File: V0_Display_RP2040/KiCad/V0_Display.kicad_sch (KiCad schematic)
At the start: 39 parts, among them J1 GPIO, J2 I2C Header, J2 USB4105-GF-A, J3 SWD, J7 USB_Header, J8 Neopixel, SW6 Kill_SW, SW7 Rotary_Enc, U1 AP2127K-3.3, U2 W25Q16JVUXIQ, U3 74LVC1G17, U4 RP2040, Y1 12MHz

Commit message: Fix Footprints
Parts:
- J2: value USB4105-GF-A -> GT-USB-7010ASV; footprint footprints:USB4105-GF-A -> Connector_USB:USB_C_Receptacle_G-Switch_GT-USB-7010ASV
- R1, R11: value 10k -> 10K
- U3: footprint V0-Display:SOT-753 -> Package_TO_SOT_SMD:SOT-23-5
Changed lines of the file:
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@@
       (effects (font (size 1.27 1.27)))
     )
-    (property "Footprint" "V0-Display:SOT-753" (at 111.76 189.23 0)
+    (property "Footprint" "Package_TO_SOT_SMD:SOT-23-5" (at 111.76 189.23 0)
       (effects (font (size 1.27 1.27)) hide)
     )
@@
       (effects (font (size 1.524 1.524)) (justify left))
     )
-    (property "Value" "USB4105-GF-A" (at 118.11 91.44 0)
+    (property "Value" "GT-USB-7010ASV" (at 118.11 91.44 0)
       (effects (font (size 1.524 1.524)) (justify left))
     )
-    (property "Footprint" "footprints:USB4105-GF-A" (at 127 91.694 0)
+    (property "Footprint" "Connector_USB:USB_C_Receptacle_G-Switch_GT-USB-7010ASV" (at 127 91.694 0)
       (effects (font (size 1.524 1.524)) hide)
     )
@@
       (effects (font (size 1.27 1.27)))
     )
-    (property "Value" "10k" (at 149.86 106.68 90)
+    (property "Value" "10K" (at 149.86 106.68 90)
       (effects (font (size 1.27 1.27)))
     )
@@
       (effects (font (size 1.27 1.27)))
     )
-    (property "Value" "10k" (at 104.14 104.14 90)
-      (effects (font (size 1.27 1.27)))
-    )
+    (property "Value" "10K" (at 104.14 104.14 90)
+      (effects (font (size 1.27 1.27)))
+    )

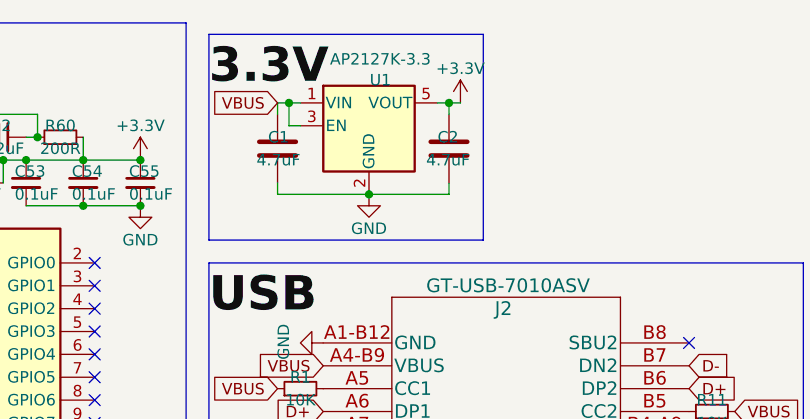
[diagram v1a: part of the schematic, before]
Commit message: Update Files
New 3.3V Regulator
"Fixed" Neopixel Level Shifter
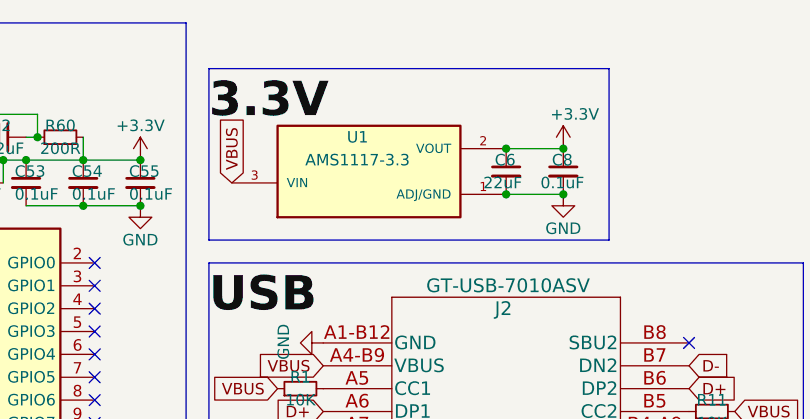
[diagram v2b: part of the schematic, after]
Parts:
- removed C1, C2: 4.7uF, Capacitor_SMD:C_0603_1608Metric, symbol Device:C
- removed U1: AP2127K-3.3, Package_TO_SOT_SMD:SOT-23-5, symbol V0_Display:AP2127K-3.3
- added C6: 22uF, Capacitor_SMD:C_0603_1608Metric, symbol Device:C_Small
- added C8: 0.1uF, Capacitor_SMD:C_0603_1608Metric, symbol Device:C_Small
- added U1: AMS1117-3.3, footprints:AMS1117-3.3, symbol AMS1117-3.3:AMS1117-3.3
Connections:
- net +3.3V: now also C6.1, C8.1, U1.2 (VOUT)
- net GND: now also C6.2, C8.2, U1.1 (ADJ/GND)
- net VCC: now also U1.3 (VIN)

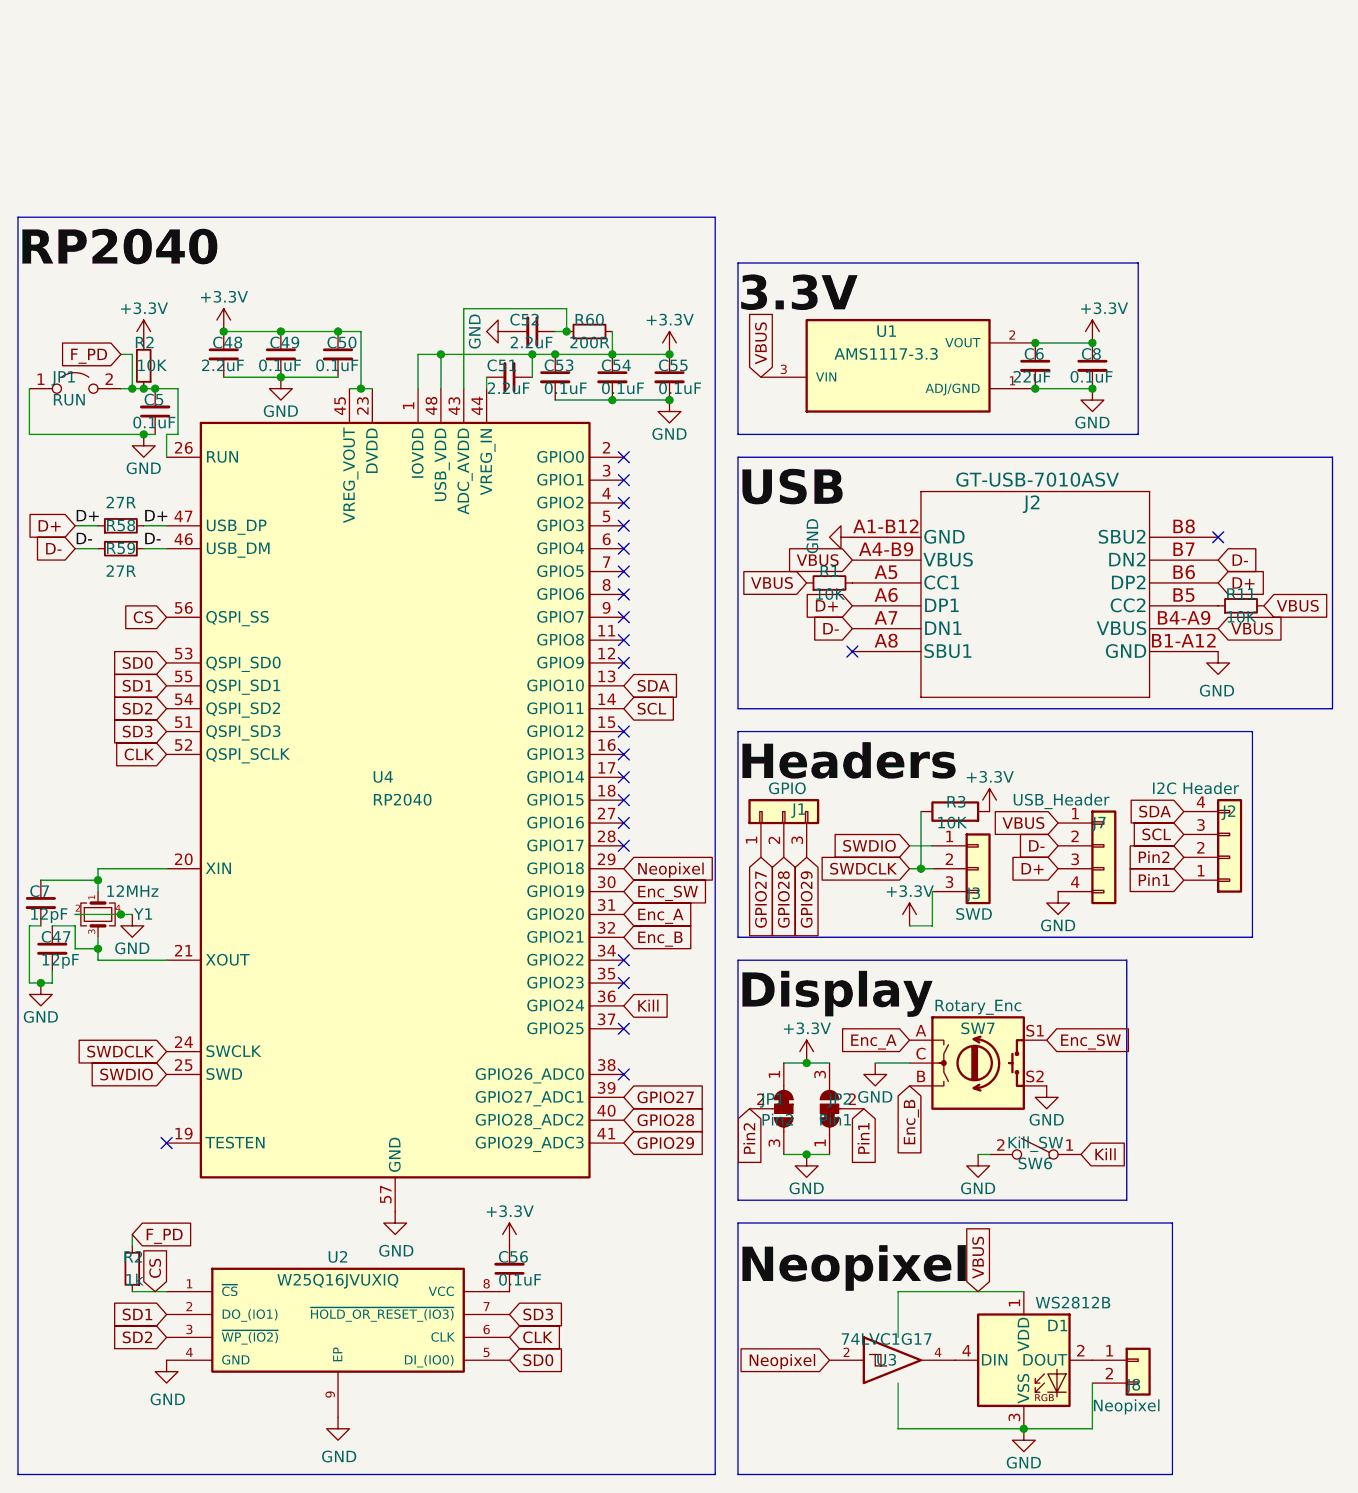
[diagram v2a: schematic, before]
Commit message: Rev 1.1
Fix Vreg-Out Problem
Change to AMS1117-3.3
22uF Input Capacitor on VBUS (5V IN)
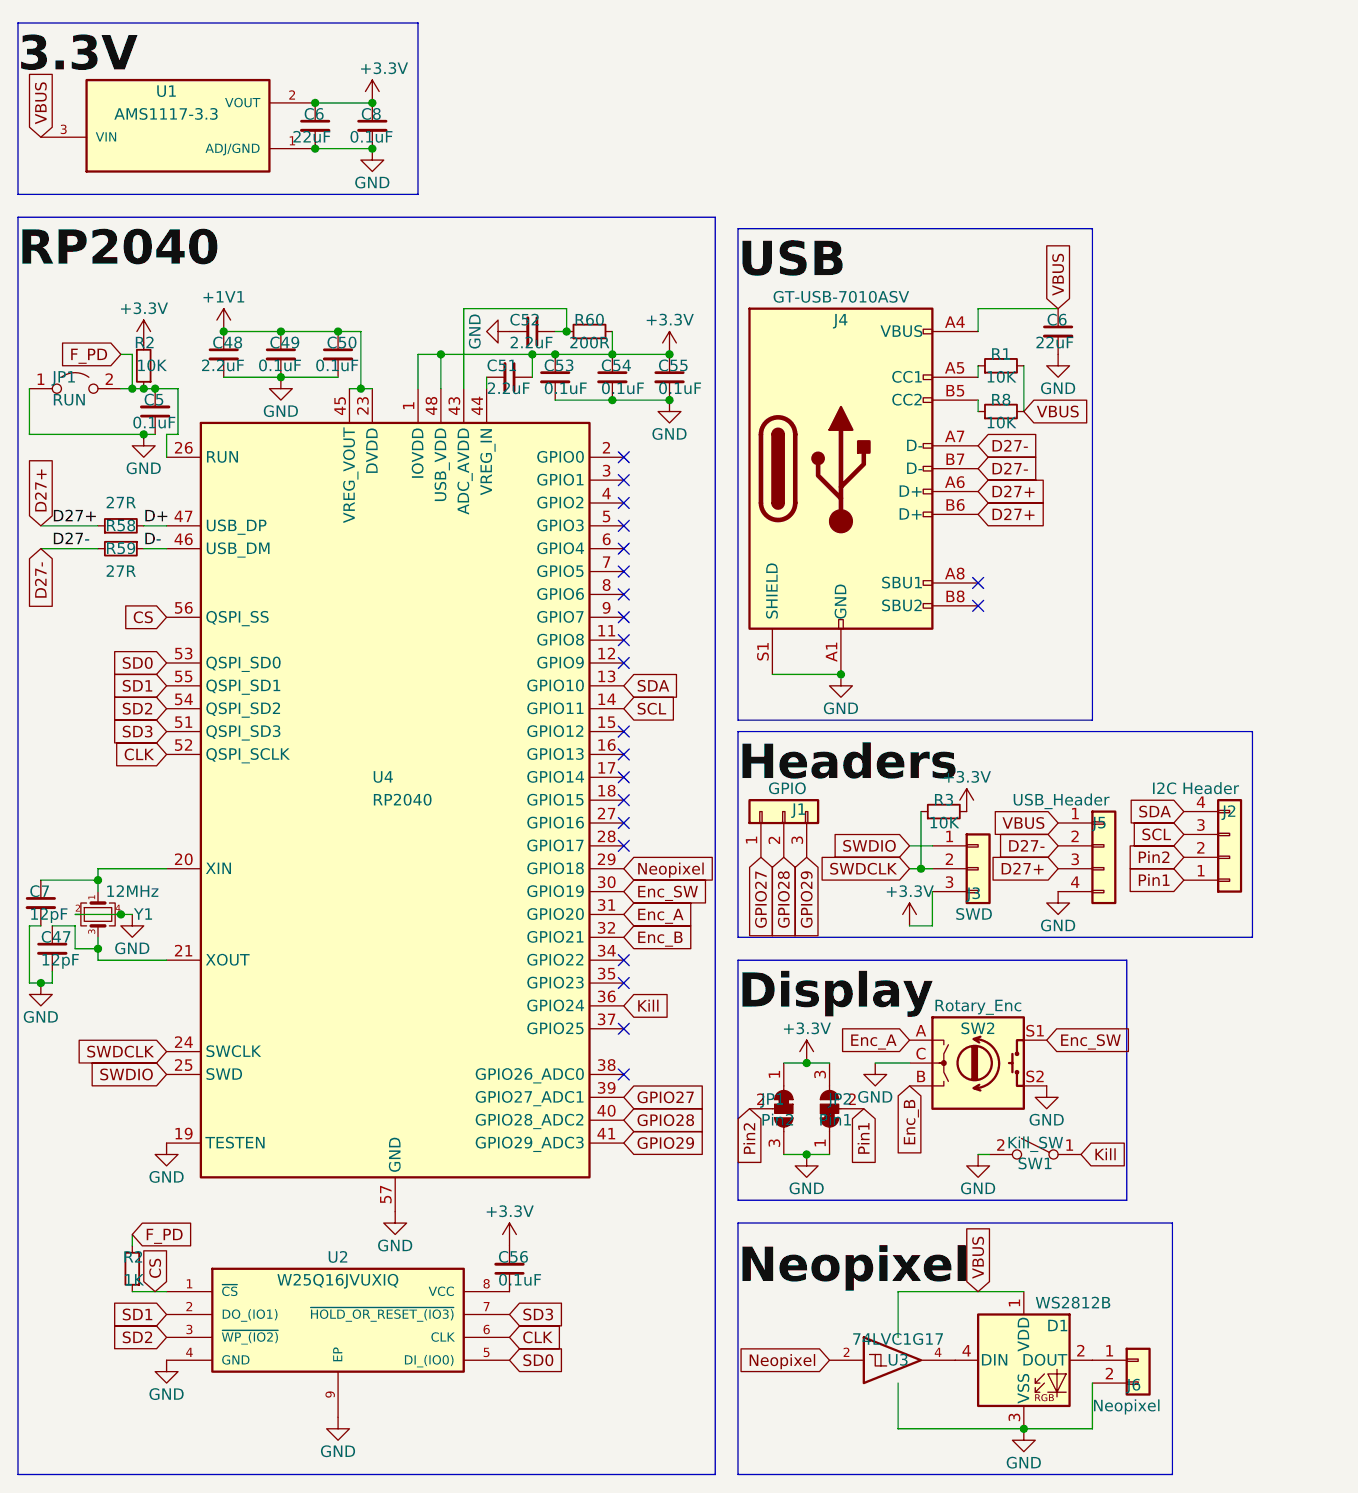
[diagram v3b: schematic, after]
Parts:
- removed J2: GT-USB-7010ASV, Connector_USB:USB_C_Receptacle_G-Switch_GT-USB-7010ASV, symbol ul_USB4105-GF-A:USB4105-GF-A
- removed R11: 10K, Resistor_SMD:R_0603_1608Metric, symbol Device:R_Small
- removed R3: 10K, Resistor_SMD:R_0603_1608Metric, symbol V0_Display:R
- added C6: 22uF, Capacitor_SMD:C_0805_2012Metric, symbol Device:C_Small
- added J4: GT-USB-7010ASV, Connector_USB:USB_C_Receptacle_G-Switch_GT-USB-7010ASV, symbol Connector:USB_C_Receptacle_USB2.0
- added R3, R8: 10K, Resistor_SMD:R_0603_1608Metric, symbol Device:R_Small
- C47, C7: LCSC (none) -> C107034
- C48, C51, C52: LCSC (none) -> C71000
- C49, C5, C50, C53, C54, C55, C56, C8: LCSC (none) -> C30926; MANUFACTURER Samsung Electro Mechanics -> (none)
- C6: footprint Capacitor_SMD:C_0603_1608Metric -> Capacitor_SMD:C_0805_2012Metric; LCSC (none) -> C2859526; MANUFACTURER Murata -> (none)
- D1: LCSC (none) -> C2843785
- J1, J3: LCSC (none) -> C429954
- J5: renamed from J7; LCSC (none) -> C2935910
- J6: renamed from J8; LCSC (none) -> C2894925
- JP1: LCSC (none) -> C118141
- R1: LCSC (none) -> C304415
- R2: value 1k -> 1K; LCSC (none) -> C110774; MANUFACTURER YAGEO -> (none)
- R2: LCSC (none) -> C304415; MANUFACTURER YAGEO -> (none)
- R58, R59: LCSC (none) -> C861276
- R60: LCSC (none) -> C8218
- SW1: renamed from SW6; LCSC (none) -> C455090
- U1: LCSC (none) -> C6186
- U2: DESCRIPTION SPIFLASH, 3V, 16M-BIT, 4KB UNIFO -> (none); HEIGHT 0.6mm -> (none); LCSC (none) -> C2843335; MANUFACTURER (none) -> Winbond; MANUFACTURER_NAME Winbond -> (none); MANUFACTURER_PART_NUMBER W25Q16JVUXIQ -> (none)
- U3: MANUFACTURER (none) -> Nexperia
- U4: LCSC (none) -> C2040; MANUFACTURER (none) -> Raspberry Pi
- Y1: LCSC (none) -> C654949
- renumbered SW7 to SW2
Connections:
- net +3.3V: now also R3.2; no longer C48.1, C49.1, C50.1, U4.23 (DVDD), U4.45 (VREG_VOUT), U4.50 (DVDD)
- net D+: no longer J5.3 (Pin_3), R58.1
- net D-: no longer J5.2 (Pin_2), R59.2
- net GND: now also U4.19 (TESTEN), C6.2, J4.A1 (GND), J4.A12 (GND), J4.B1 (GND), J4.B12 (GND), J4.S1 (SHIELD)
- net SWDCLK: now also R3.1
- net VCC: now also R1.2, C6.1, J4.A4 (VBUS), J4.A9 (VBUS), J4.B4 (VBUS), J4.B9 (VBUS), R8.2; no longer R1.1
- new net: J4.A5 (CC1), R1.1
- new net: J4.B5 (CC2), R8.1
- new net +1V1: C48.1, C49.1, C50.1, U4.23 (DVDD), U4.45 (VREG_VOUT), U4.50 (DVDD)
- new net D27+: J4.A6 (D+), J4.B6 (D+), J5.3 (Pin_3), R58.1
- new net D27-: J4.A7 (D-), J4.B7 (D-), J5.2 (Pin_2), R59.2
- no-connect marks 23 -> 22
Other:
- moved on the sheet: C6, C8, U1
